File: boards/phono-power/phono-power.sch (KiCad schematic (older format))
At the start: 19 parts, among them J1 Conn_01x05, J2 Conn_01x06_Female, J3 Conn_01x06_Female, SW1 SW_SPST_GND, T1 Transformer_272X, U1 6CA4

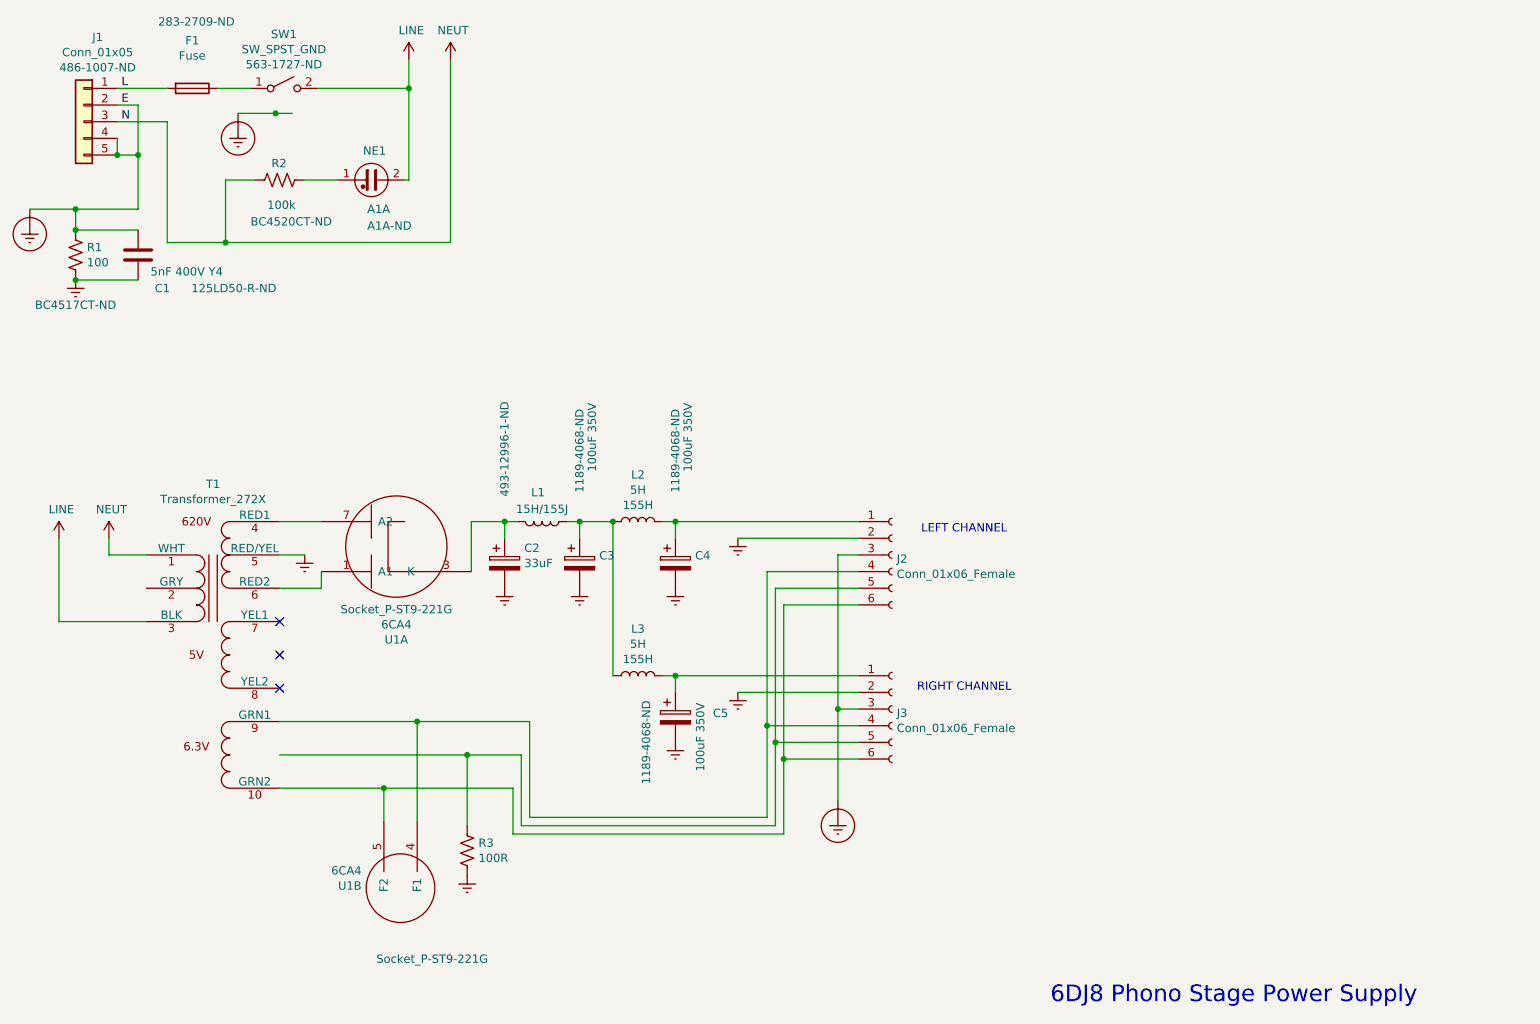
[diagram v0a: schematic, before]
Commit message: Pause to consider board sizes
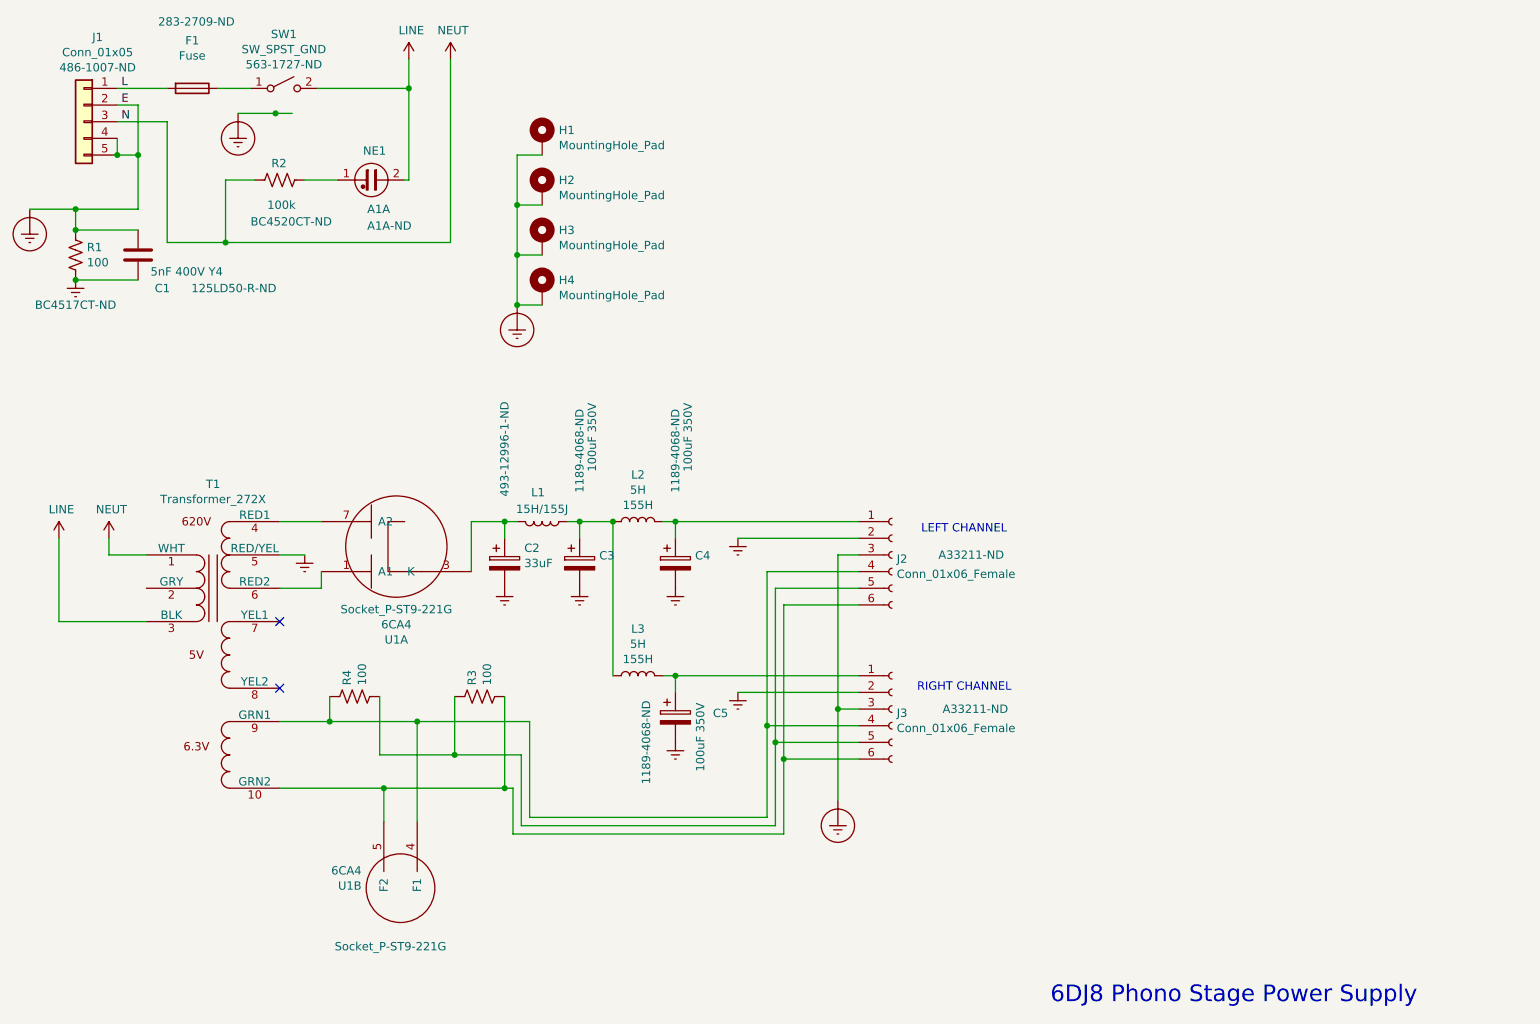
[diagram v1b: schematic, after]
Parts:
- added H1, H2, H3, H4: MountingHole_Pad, MountingHolesInch:Mtg6-32, symbol Mechanical:MountingHole_Pad
- added R4: 100, Resistor_THT:R_Axial_DIN0414_L11.9mm_D4.5mm_P15.24mm_Horizontal, symbol Device:R_US
- J2, J3: footprint (none) -> Connector_Molex:Molex_Micro-Fit_3.0_43650-0615_1x06_P3.00mm_Vertical; CatNo (none) -> A33211-ND; Vendor (none) -> DigiKey
- R3: value 100R -> 100; footprint (none) -> Resistor_THT:R_Axial_DIN0414_L11.9mm_D4.5mm_P15.24mm_Horizontal; CatNo (none) -> BC4517CT-ND; Vendor (none) -> DigiKey
- T1: footprint (none) -> my-connectors:Hammond-272X; CatNo (none) -> HM5014-ND; Vendor (none) -> DigiKey
- U1: footprint Valve:Valve_Noval_P -> my-capacitors:P-ST9-700-PC
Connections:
- net Earth: no longer R3.2
- net Earth_Protective: now also H1.1, H2.1, H3.1, H4.1
- net at J2.6 (Pin_6), J3.6 (Pin_6), T1.10 (GRN2)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: now also R3.2
- net at J2.4 (Pin_4), J3.4 (Pin_4), T1.9 (GRN1)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: now also R4.1
- net at J2.5 (Pin_5), J3.5 (Pin_5), R3.1: now also R4.2
- no-connect marks 3 -> 2
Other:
- moved on the sheet: R3
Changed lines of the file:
@@
 F 0 "U1" H 3175 4559 50  0000 C CNN
 F 1 "6CA4" H 3175 4468 50  0000 C CNN
-F 2 "Valve:Valve_Noval_P" H 2725 4150 50  0001 C CNN
+F 2 "my-capacitors:P-ST9-700-PC" H 2725 4150 50  0001 C CNN
 F 3 "" H 2725 4150 50  0001 C CNN
 F 4 "Socket_P-ST9-221G" H 3175 4377 50  0000 C CNN "CatNo"
@@
 F 0 "T1" H 2075 4475 50  0000 C CNN
 F 1 "Transformer_272X" H 2075 4384 50  0000 C CNN
-F 2 "" H 2075 3850 50  0001 C CNN
+F 2 "my-connectors:Hammond-272X" H 2075 3850 50  0001 C CNN
 F 3 "~" H 2075 3850 50  0001 C CNN
+F 4 "HM5014-ND" H 2075 4050 50  0001 C CNN "CatNo"
+F 5 "DigiKey" H 2075 4050 50  0001 C CNN "Vendor"
 	1    2075 4050
 	1    0    0    -1
@@
 F 0 "J2" H 6178 4026 50  0000 L CNN
 F 1 "Conn_01x06_Female" H 6178 3935 50  0000 L CNN
-F 2 "" H 6150 4050 50  0001 C CNN
+F 2 "Connector_Molex:Molex_Micro-Fit_3.0_43650-0615_1x06_P3.00mm_Vertical" H 6150 4050 50  0001 C CNN
 F 3 "~" H 6150 4050 50  0001 C CNN
+F 4 "A33211-ND" H 6625 4050 50  0000 C CNN "CatNo"
+F 5 "DigiKey" H 6150 4050 50  0001 C CNN "Vendor"
 	1    6150 4050
 	1    0    0    -1
@@
 F 0 "J3" H 6178 4951 50  0000 L CNN
 F 1 "Conn_01x06_Female" H 6178 4860 50  0000 L CNN
-F 2 "" H 6150 4975 50  0001 C CNN
+F 2 "Connector_Molex:Molex_Micro-Fit_3.0_43650-0615_1x06_P3.00mm_Vertical" H 6150 4975 50  0001 C CNN
 F 3 "~" H 6150 4975 50  0001 C CNN
+F 4 "A33211-ND" H 6650 4975 50  0000 C CNN "CatNo"
+F 5 "DigiKey" H 6150 4975 50  0001 C CNN "Vendor"
 	1    6150 4975
 	1    0    0    -1
@@
 	3975 5050 3300 5050
 Wire Wire Line
-	2475 5250 3600 5250
-Wire Wire Line
 	3925 5250 3925 5675
 Wire Wire Line
@@
 	3875 5725 3875 5450
 Wire Wire Line
-	3875 5450 3100 5450
+	3875 5450 3825 5450
 Wire Wire Line
 	5400 5075 5400 4150
@@
 Connection ~ 5825 4975
 NoConn ~ 2475 4450
-NoConn ~ 2475 4650
 NoConn ~ 2475 4850
 $Comp
@@
 F 0 "U1" H 4434 6036 50  0000 L CNN
 F 1 "6CA4" H 4434 5945 50  0000 L CNN
-F 2 "Valve:Valve_Noval_P" H 3800 5850 50  0001 C CNN
+F 2 "my-capacitors:P-ST9-700-PC" H 3800 5850 50  0001 C CNN
 F 3 "" H 3800 5850 50  0001 C CNN
-F 4 "Socket_P-ST9-221G" H 3675 6475 50  0000 L CNN "CatNo"
+F 4 "Socket_P-ST9-221G" H 3925 6400 50  0000 L CNN "CatNo"
 	2    3700 5850
 	-1   0    0    1
@@
 Connection ~ 3300 5050
 Wire Wire Line
-	3300 5050 2475 5050
+	3300 5050 2775 5050
 $Comp
 L Device:R_US R3
 U 1 1 608F6885
-P 3600 5825
-F 0 "R3" H 3668 5871 50  0000 L CNN
-F 1 "100R" H 3668 5780 50  0000 L CNN
-F 2 "" V 3640 5815 50  0001 C CNN
-F 3 "~" H 3600 5825 50  0001 C CNN
-	1    3600 5825
-	1    0    0    -1
-$EndComp
-Wire Wire Line
-	3600 5675 3600 5250
-Connection ~ 3600 5250
-Wire Wire Line
-	3600 5250 3925 5250
-$Comp
-L power:Earth #PWR09
-U 1 1 608F8FEA
-P 3600 5975
-F 0 "#PWR09" H 3600 5725 50  0001 C CNN
-F 1 "Earth" H 3600 5825 50  0001 C CNN
-F 2 "" H 3600 5975 50  0001 C CNN
-F 3 "~" H 3600 5975 50  0001 C CNN
-	1    3600 5975
-	1    0    0    -1
+P 3675 4900
+F 0 "R3" H 3743 4946 50  0000 L CNN
+F 1 "100" H 3743 4855 50  0000 L CNN
+F 2 "Resistor_THT:R_Axial_DIN0414_L11.9mm_D4.5mm_P15.24mm_Horizontal" V 3715 4890 50  0001 C CNN
+F 3 "~" H 3675 4900 50  0001 C CNN
+F 4 "BC4517CT-ND" H 3675 4900 50  0001 C CNN "CatNo"
+F 5 "DigiKey" H 3675 4900 50  0001 C CNN "Vendor"
+	1    3675 4900
+	0    -1   -1   0
 $EndComp
 Text Notes 6325 3925 0    50   ~ 0
@@
 Text Notes 6300 4875 0    50   ~ 0
 RIGHT CHANNEL\n
+$Comp
+L Device:R_US R4
+U 1 1 608F726D
+P 2925 4900
+F 0 "R4" H 2993 4946 50  0000 L CNN
+F 1 "100" H 2993 4855 50  0000 L CNN
+F 2 "Resistor_THT:R_Axial_DIN0414_L11.9mm_D4.5mm_P15.24mm_Horizontal" V 2965 4890 50  0001 C CNN
+F 3 "~" H 2925 4900 50  0001 C CNN
+F 4 "BC4517CT-ND" H 2925 4900 50  0001 C CNN "CatNo"
+F 5 "DigiKey" H 2925 4900 50  0001 C CNN "Vendor"
+	1    2925 4900
+	0    -1   -1   0
+$EndComp
+Wire Wire Line
+	2775 4900 2775 5050
+Connection ~ 2775 5050
+Wire Wire Line
+	2775 5050 2475 5050
+Wire Wire Line
+	3075 4900 3075 5250
+Wire Wire Line
+	3075 5250 3525 5250
+Wire Wire Line
+	3525 4900 3525 5250
+Connection ~ 3525 5250
+Wire Wire Line
+	3525 5250 3925 5250
+Wire Wire Line
+	3825 4900 3825 5450
+Connection ~ 3825 5450
+Wire Wire Line
+	3825 5450 3100 5450
+$Comp
+L Mechanical:MountingHole_Pad H1
+U 1 1 608F7FF6
+P 4050 1550
+F 0 "H1" H 4150 1599 50  0000 L CNN
+F 1 "MountingHole_Pad" H 4150 1508 50  0000 L CNN
+F 2 "MountingHolesInch:Mtg6-32" H 4050 1550 50  0001 C CNN
+F 3 "~" H 4050 1550 50  0001 C CNN
+	1    4050 1550
+	1    0    0    -1
+$EndComp
+$Comp
+L Mechanical:MountingHole_Pad H2
+U 1 1 608F8DF7
+P 4050 1850
+F 0 "H2" H 4150 1899 50  0000 L CNN
+F 1 "MountingHole_Pad" H 4150 1808 50  0000 L CNN
+F 2 "MountingHolesInch:Mtg6-32" H 4050 1850 50  0001 C CNN
+F 3 "~" H 4050 1850 50  0001 C CNN
+	1    4050 1850
+	1    0    0    -1
+$EndComp
+$Comp
+L Mechanical:MountingHole_Pad H3
+U 1 1 608F9601
+P 4050 2150
+F 0 "H3" H 4150 2199 50  0000 L CNN
+F 1 "MountingHole_Pad" H 4150 2108 50  0000 L CNN
+F 2 "MountingHolesInch:Mtg6-32" H 4050 2150 50  0001 C CNN
+F 3 "~" H 4050 2150 50  0001 C CNN
+	1    4050 2150
+	1    0    0    -1
+$EndComp
+$Comp
+L Mechanical:MountingHole_Pad H4
+U 1 1 608F9D7C
+P 4050 2450
+F 0 "H4" H 4150 2499 50  0000 L CNN
+F 1 "MountingHole_Pad" H 4150 2408 50  0000 L CNN
+F 2 "MountingHolesInch:Mtg6-32" H 4050 2450 50  0001 C CNN
+F 3 "~" H 4050 2450 50  0001 C CNN
+	1    4050 2450
+	1    0    0    -1
+$EndComp
+Wire Wire Line
+	4050 1650 3900 1650
+Wire Wire Line
+	3900 1650 3900 1950
+Wire Wire Line
+	3900 1950 4050 1950
+Wire Wire Line
+	3900 1950 3900 2250
+Wire Wire Line
+	3900 2250 4050 2250
+Connection ~ 3900 1950
+Wire Wire Line
+	3900 2250 3900 2550
+Wire Wire Line
+	3900 2550 4050 2550
+Connection ~ 3900 2250
+$Comp
+L power:Earth_Protective #PWR09
+U 1 1 60900DF7
+P 3900 2550
+F 0 "#PWR09" H 4150 2300 50  0001 C CNN
+F 1 "Earth_Protective" H 4350 2400 50  0001 C CNN
+F 2 "" H 3900 2450 50  0001 C CNN
+F 3 "~" H 3900 2450 50  0001 C CNN
+	1    3900 2550
+	1    0    0    -1
+$EndComp
+Connection ~ 3900 2550
 $EndSCHEMATC
